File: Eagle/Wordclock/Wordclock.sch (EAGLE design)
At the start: 281 parts, among them IC1 MEGA8-P, Q3 SUP75N06-08

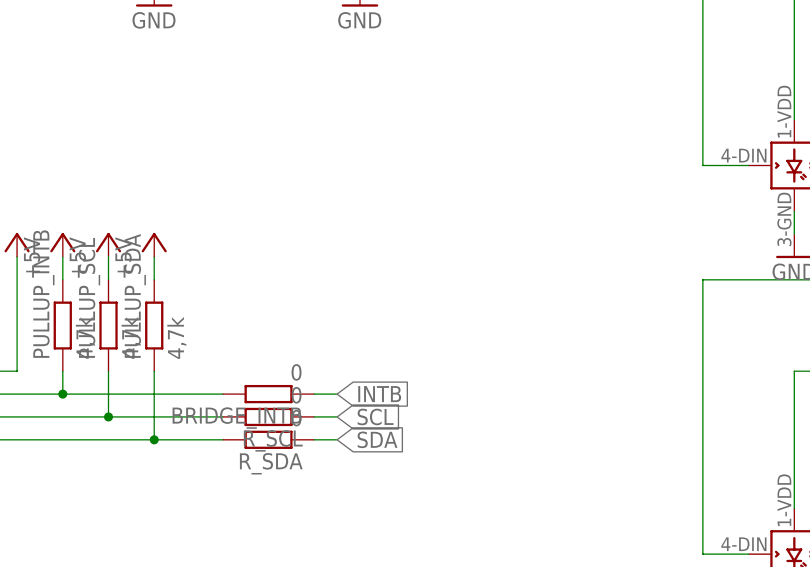
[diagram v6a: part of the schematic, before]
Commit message: Eagle: Pullups I2C geroutet und Befestigungslöcher auf 3,2 angepasst
Bohrergröße für Platine nun M3 fein nach Tabelle unter
https://de.wikipedia.org/wiki/Metrisches_ISO-Gewinde
Pullup_SCL und Pullup_SDA nun im Layout eingefügt
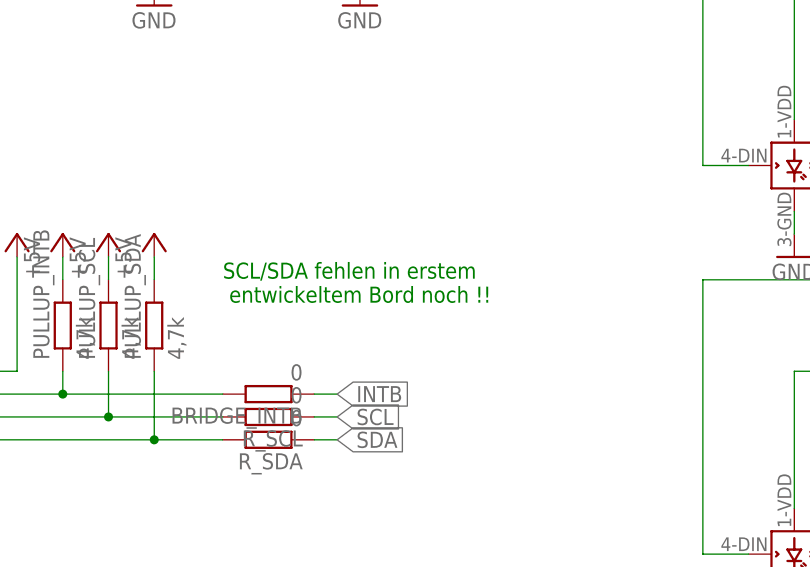
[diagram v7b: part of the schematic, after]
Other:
- note added: "SCL/SDA fehlen in erstem entwickeltem Bord noch !!"
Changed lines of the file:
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@@
 Schaltungsteile
 z.B. Bewegungsmelder</text>
+<text x="-2.54" y="-208.28" size="1.778" layer="91">SCL/SDA fehlen in erstem
+ entwickeltem Bord noch !!</text>
 </plain>
 <instances>
@@
 </segment>
 <segment>
-<pinref part="PULLUP_SDA" gate="G$1" pin="2"/>
 <pinref part="P+13" gate="1" pin="+5V"/>
 <wire x1="-10.16" y1="-205.74" x2="-10.16" y2="-203.2" width="0.1524" layer="91"/>
+<pinref part="PULLUP_SDA" gate="G$1" pin="2"/>
 </segment>
 <segment>
 <pinref part="P+12" gate="1" pin="+5V"/>
-<pinref part="PULLUP_SCL" gate="G$1" pin="2"/>
 <wire x1="-15.24" y1="-203.2" x2="-15.24" y2="-205.74" width="0.1524" layer="91"/>
+<pinref part="PULLUP_SCL" gate="G$1" pin="2"/>
 </segment>
 </net>
@@
 <pinref part="R_SCL" gate="G$1" pin="2"/>
 <wire x1="-2.54" y1="-220.98" x2="-15.24" y2="-220.98" width="0.1524" layer="91"/>
-<pinref part="PULLUP_SCL" gate="G$1" pin="1"/>
 <wire x1="-15.24" y1="-220.98" x2="-27.94" y2="-220.98" width="0.1524" layer="91"/>
 <wire x1="-15.24" y1="-215.9" x2="-15.24" y2="-220.98" width="0.1524" layer="91"/>
 <junction x="-15.24" y="-220.98"/>
+<pinref part="PULLUP_SCL" gate="G$1" pin="1"/>
 </segment>
 </net>
@@
 <pinref part="R_SDA" gate="G$1" pin="2"/>
 <wire x1="-2.54" y1="-223.52" x2="-10.16" y2="-223.52" width="0.1524" layer="91"/>
-<pinref part="PULLUP_SDA" gate="G$1" pin="1"/>
 <wire x1="-10.16" y1="-223.52" x2="-27.94" y2="-223.52" width="0.1524" layer="91"/>
 <wire x1="-10.16" y1="-215.9" x2="-10.16" y2="-223.52" width="0.1524" layer="91"/>
 <junction x="-10.16" y="-223.52"/>
+<pinref part="PULLUP_SDA" gate="G$1" pin="1"/>
 </segment>
 </net>

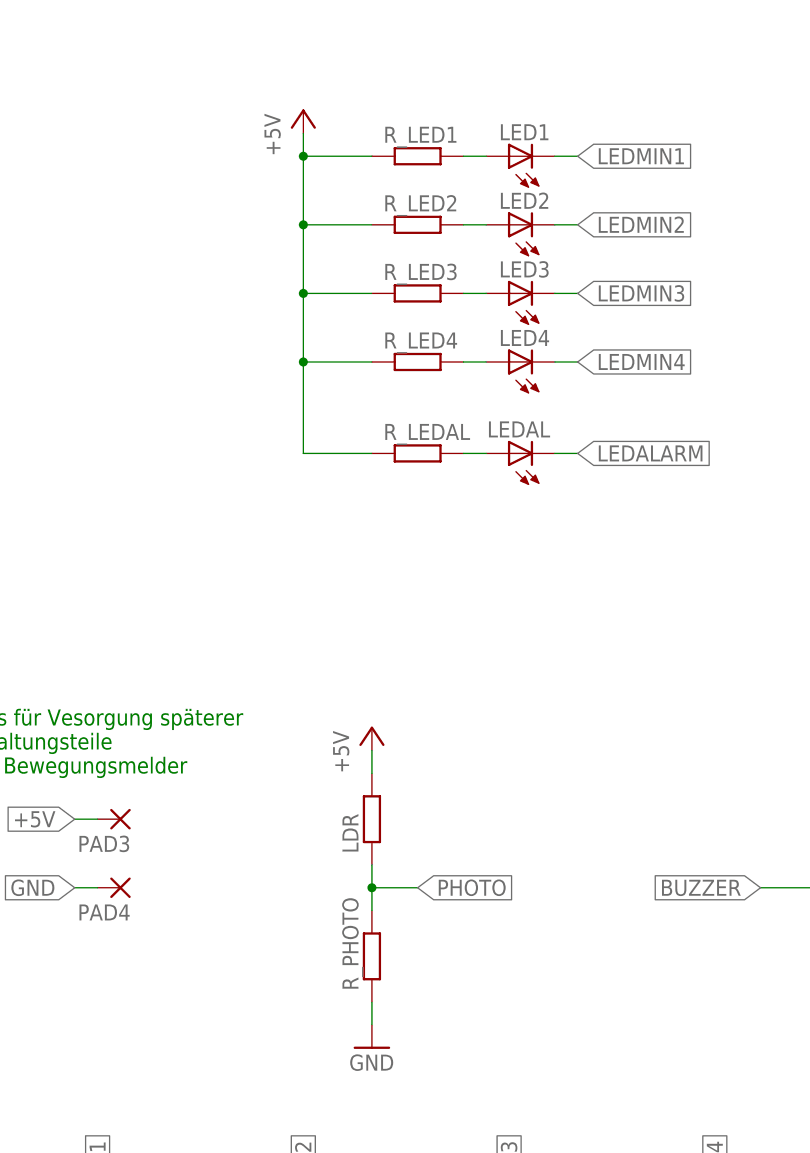
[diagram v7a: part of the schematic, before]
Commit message: Bauteilliste exportiert
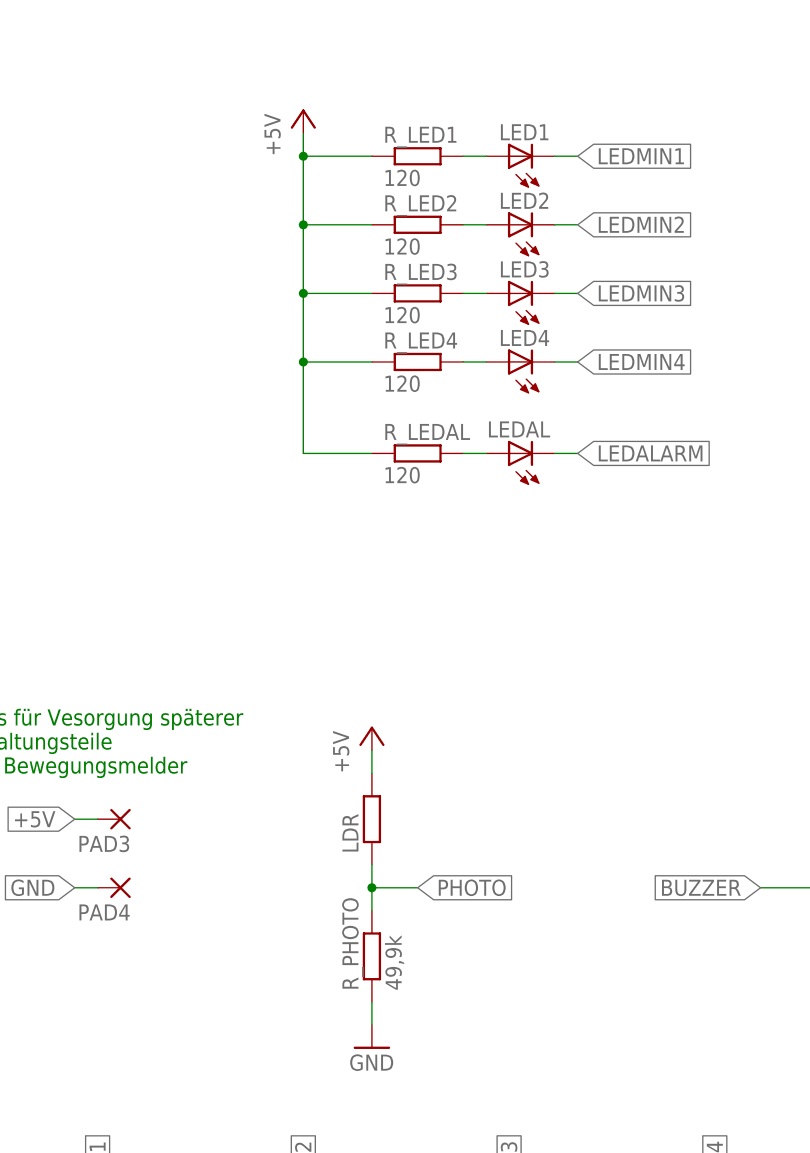
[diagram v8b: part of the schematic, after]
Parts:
- R_LED1, R_LED2, R_LED3, R_LED4, R_LEDAL: value (none) -> 120
- R_PHOTO: value (none) -> 49,9k
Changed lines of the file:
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@@
 <part name="PULLUP_INTA" library="rcl" deviceset="R-EU_" device="R1206" value="4,7k"/>
 <part name="PULLUP_INTB" library="rcl" deviceset="R-EU_" device="R1206" value="4,7k"/>
-<part name="R_LED1" library="rcl" deviceset="R-EU_" device="M1206"/>
-<part name="R_LED2" library="rcl" deviceset="R-EU_" device="M1206"/>
-<part name="R_LED3" library="rcl" deviceset="R-EU_" device="M1206"/>
-<part name="R_LED4" library="rcl" deviceset="R-EU_" device="M1206"/>
+<part name="R_LED1" library="rcl" deviceset="R-EU_" device="M1206" value="120"/>
+<part name="R_LED2" library="rcl" deviceset="R-EU_" device="M1206" value="120"/>
+<part name="R_LED3" library="rcl" deviceset="R-EU_" device="M1206" value="120"/>
+<part name="R_LED4" library="rcl" deviceset="R-EU_" device="M1206" value="120"/>
 <part name="LED1" library="led" deviceset="LED" device="CHIPLED_1206"/>
 <part name="LED2" library="led" deviceset="LED" device="CHIPLED_1206"/>
@@
 <part name="LED4" library="led" deviceset="LED" device="CHIPLED_1206"/>
 <part name="LEDAL" library="led" deviceset="LED" device="CHIPLED_1206"/>
-<part name="R_LEDAL" library="rcl" deviceset="R-EU_" device="M1206"/>
+<part name="R_LEDAL" library="rcl" deviceset="R-EU_" device="M1206" value="120"/>
 <part name="IC1" library="atmel" deviceset="MEGA8-P" device=""/>
 <part name="GND222" library="supply1" deviceset="GND" device=""/>
@@
 <part name="P+7" library="supply1" deviceset="+5V" device=""/>
 <part name="LDR" library="rcl" deviceset="R-EU_" device="0204/5"/>
-<part name="R_PHOTO" library="rcl" deviceset="R-EU_" device="M1206"/>
+<part name="R_PHOTO" library="rcl" deviceset="R-EU_" device="M1206" value="49,9k"/>
 <part name="P+8" library="supply1" deviceset="+5V" device=""/>
 <part name="GND229" library="supply1" deviceset="GND" device=""/>
@@
 </sheet>
 </sheets>
+<errors>
+</errors>
 </schematic>
 </drawing>
